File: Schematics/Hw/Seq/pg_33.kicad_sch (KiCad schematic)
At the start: 11 parts, among them U3401 F04, U3402 F02, U3403 F37, U3404 F158, U3405 F158, U3406 F158, U3407 F381, U3408 F381, U3409 F381, U3410 F381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

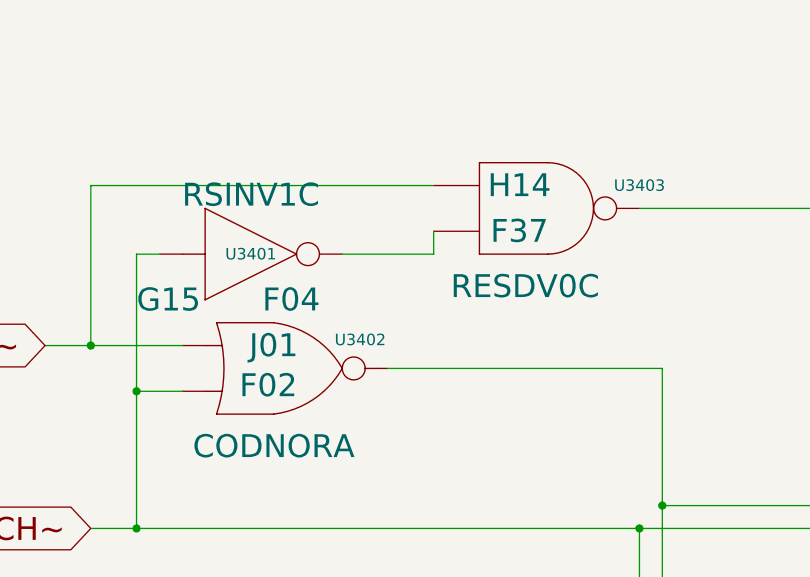
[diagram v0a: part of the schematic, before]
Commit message: Upgrade to KiCad9
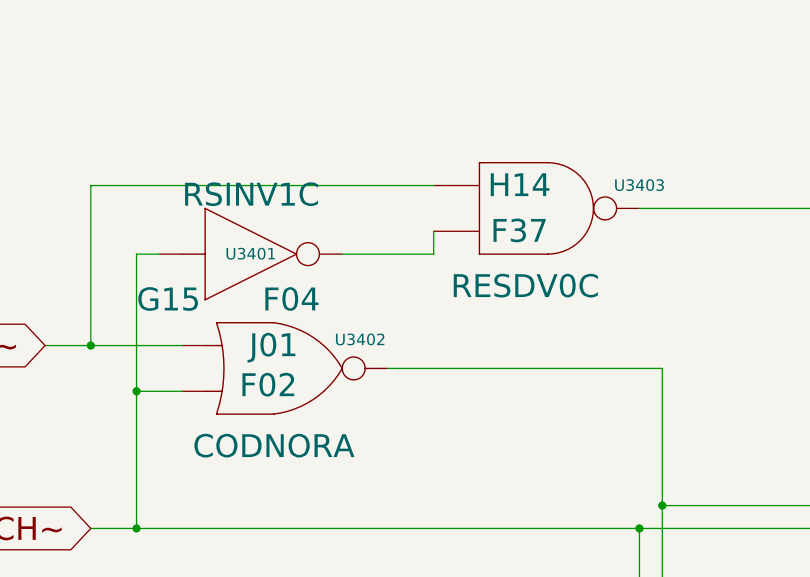
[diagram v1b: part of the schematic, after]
